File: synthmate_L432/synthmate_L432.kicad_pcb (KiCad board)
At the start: 2 copper layers, 5 parts, among them U1 STM32L432KCUx, U3 MIC5365-1.0YC5

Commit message: pcb_v1
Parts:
- added C3: 1uF, Capacitor_SMD:C_1206_3216Metric, F.Cu at (93.6, 54.4)
- added C4: 1uF, Capacitor_SMD:C_1206_3216Metric, F.Cu at (105.8, 56.7)
- added C5: 100nF, Capacitor_SMD:C_1206_3216Metric, F.Cu at (110.9, 56.8)
- added J1: USB_C_synthmate, Connector_USB:USB_C_Receptacle_GCT_USB4105-xx-A_16P_TopMnt_Horizontal, F.Cu at (94.7, 47.0)
- added J3: USB_C_connector_board, Connector_USB:USB_C_Receptacle_GCT_USB4105-xx-A_16P_TopMnt_Horizontal, F.Cu at (161.2, 47.2)
- added J5: Conn_01x16, Connector_PinSocket_2.54mm:PinSocket_1x15_P2.54mm_Vertical, F.Cu at (92.8, 60.2)
- added J6: Conn_01x13, Connector_PinSocket_2.54mm:PinSocket_1x13_P2.54mm_Vertical, F.Cu at (123.2, 33.8)
- added J7: Conn_01x04, Connector_PinSocket_2.54mm:PinSocket_1x04_P2.54mm_Vertical, F.Cu at (150.6, 43.3)
- added R1: 10k, Resistor_SMD:R_0805_2012Metric_Pad1.20x1.40mm_HandSolder, F.Cu at (116.0, 55.3)
- added R2: 5k1, Resistor_SMD:R_0805_2012Metric_Pad1.20x1.40mm_HandSolder, F.Cu at (92.5, 38.8)
- added R3: 5k1, Resistor_SMD:R_0805_2012Metric_Pad1.20x1.40mm_HandSolder, F.Cu at (96.0, 38.9)
- added R4: 1k, Resistor_SMD:R_0805_2012Metric_Pad1.20x1.40mm_HandSolder, F.Cu at (127.5, 38.0)
- added R5: 10k, Resistor_SMD:R_0805_2012Metric_Pad1.20x1.40mm_HandSolder, F.Cu at (116.3, 38.2)
- added SW1: RotaryEncoder_Switch, Rotary_Encoder:RotaryEncoder_Bourns_Vertical_PEC12R-3x17F-Sxxxx, F.Cu at (128.8, 44.5)
- added SW2: SW_Push, Button_Switch_THT:SW_TH_Tactile_Omron_B3F-10xx, F.Cu at (101.5, 50.2)
- added SW3: SW_Push, Button_Switch_THT:SW_TH_Tactile_Omron_B3F-10xx, F.Cu at (120.0, 50.2)
- added U2: USBLC6-2SC6, Package_TO_SOT_SMD:SOT-23-6, F.Cu at (106.0, 38.8)
- added U4: USBLC6-2SC6, Package_TO_SOT_SMD:SOT-23-6, F.Cu at (121.3, 55.5)
- C1: value 16V/47uF Tantalum -> 16V/47uF
- moved C2 74.9 mm to (100.7, 38.9)
- moved U3 67.5 mm to (98.1, 55.5)
- moved D1 63.0 mm to (121.8, 38.8)
- moved C1 58.8 mm to (105.7, 53.6), turned to 180 degrees
- moved U1 56.4 mm to (113.5, 45.9)
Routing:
- net 3V3: track 0.00 -> 124.1 mm, vias 0 -> 3
- net BOOT0: track 0.00 -> 110.6 mm, vias 0 -> 2
- net enc_A: track 0.00 -> 95.9 mm
- net USB_DM: track 0.00 -> 63.5 mm, vias 0 -> 1
- net NRST: track 0.00 -> 54.0 mm
- net enc_B: track 0.00 -> 53.0 mm, vias 0 -> 1
- net LPUART_TX: track 0.00 -> 47.6 mm, vias 0 -> 1
- net 5V: track 0.00 -> 45.0 mm, vias 0 -> 2
- net USB_DP: track 0.00 -> 37.0 mm, vias 0 -> 2
- net pushbutton_B: track 0.00 -> 32.3 mm, vias 0 -> 1
- net Net-(J1-SBU2): track 0.00 -> 31.9 mm
- net LPUART_RX: track 0.00 -> 31.5 mm, vias 0 -> 2
- net LED: track 0.00 -> 29.5 mm, vias 0 -> 1
- net adaptor_GND: track 0.00 -> 28.5 mm
- net Net-(J1-SBU1): track 0.00 -> 26.6 mm
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- added copper zone on B.Cu, net GND
- added copper zone on F.Cu, net GND
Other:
- board outline added: 74 x 30 mm
- board text added: "pcb cut"

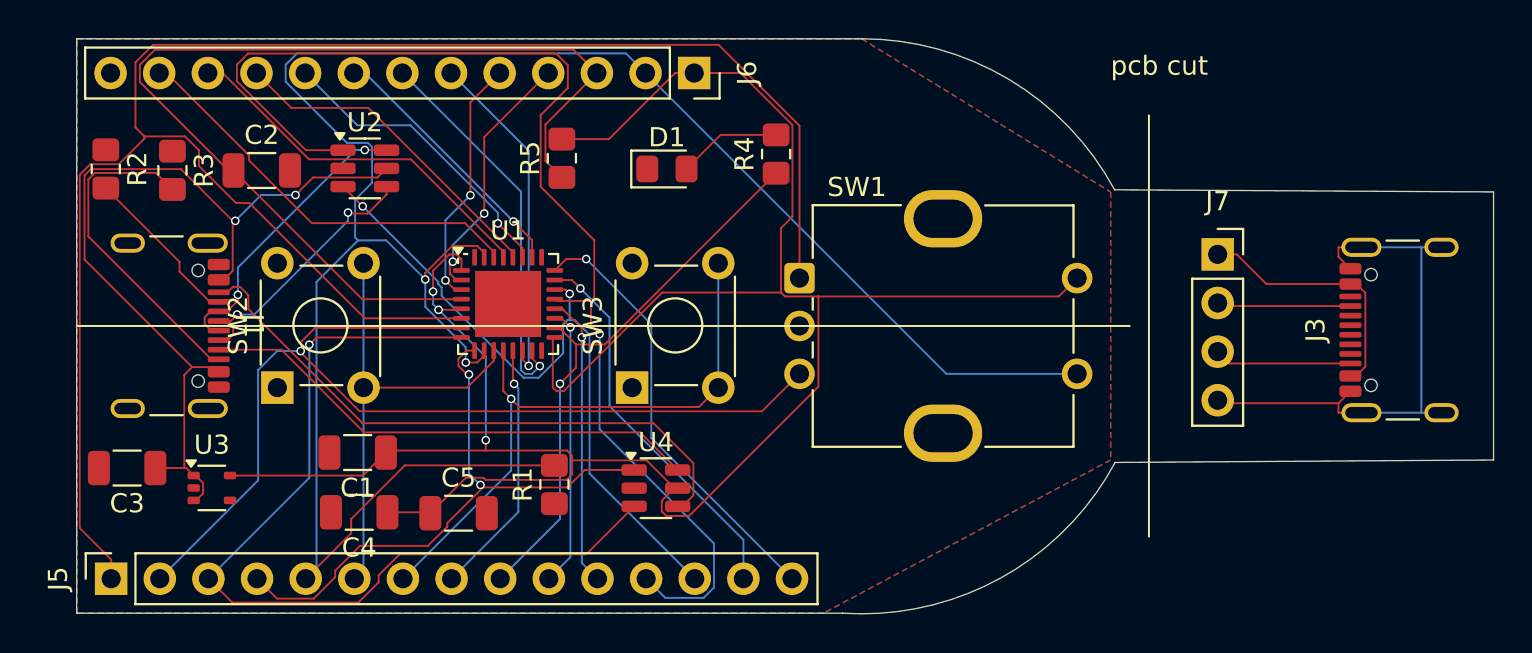
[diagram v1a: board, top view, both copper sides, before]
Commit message: switch to 4 layers, top layer signals routed
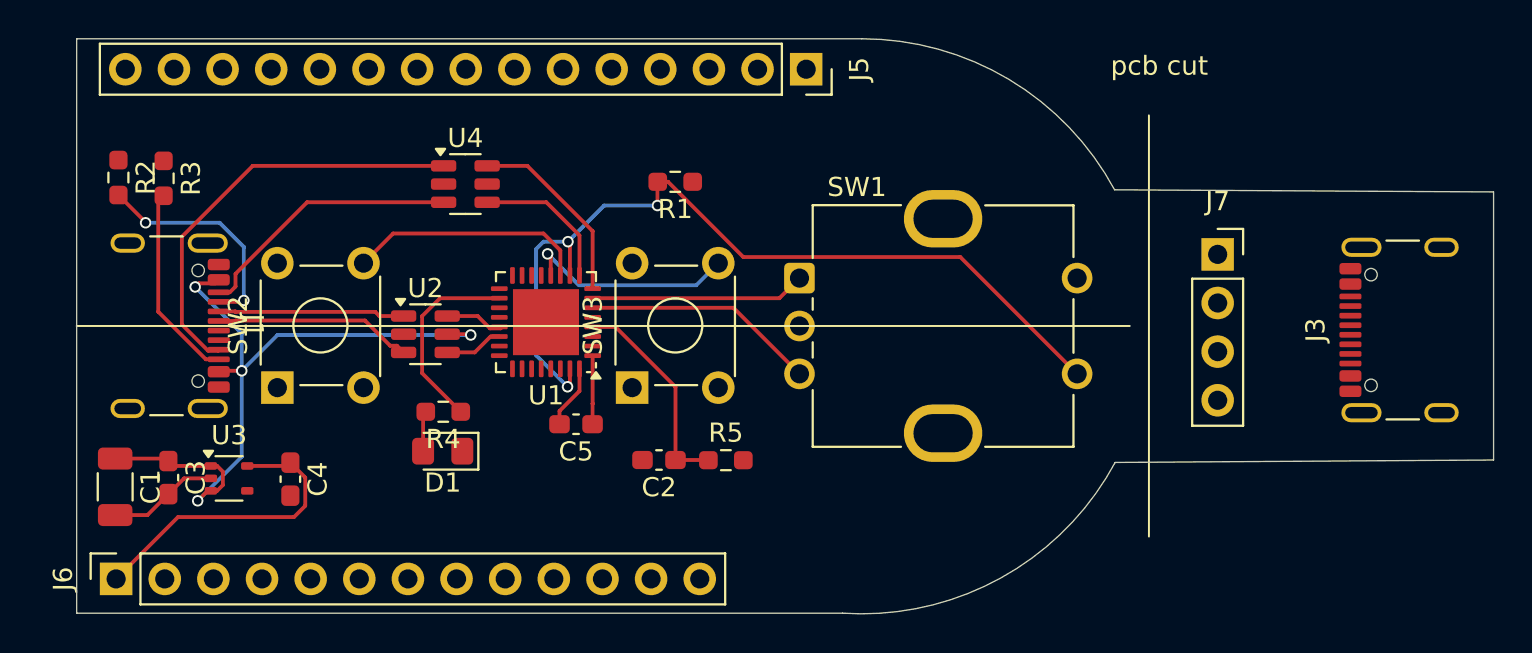
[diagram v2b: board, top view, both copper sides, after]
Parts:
- C2, C3, C4, C5: footprint Capacitor_SMD:C_1206_3216Metric -> Capacitor_SMD:C_0603_1608Metric_Pad1.08x0.95mm_HandSolder
- R1, R2, R3, R4, R5: footprint Resistor_SMD:R_0805_2012Metric_Pad1.20x1.40mm_HandSolder -> Resistor_SMD:R_0603_1608Metric_Pad0.98x0.95mm_HandSolder
- moved J5 45.0 mm to (129.1, 33.6), turned to -90 degrees
- moved J6 40.1 mm to (93.1, 60.2), turned to 90 degrees
- moved C2 25.7 mm to (121.4, 54.0), turned to 180 degrees
- moved R4 22.0 mm to (110.1, 51.5), turned to 180 degrees
- moved D1 18.8 mm to (110.1, 53.5), turned to 180 degrees
- moved U4 18.7 mm to (111.3, 39.6)
- moved R5 17.9 mm to (124.9, 54.0), turned to 0 degrees
- moved R1 17.0 mm to (122.3, 39.5), turned to 180 degrees
- moved C1 12.8 mm to (93.0, 55.4), turned to -90 degrees
- moved U2 9.22 mm to (109.2, 47.4)
- moved C5 7.70 mm to (117.1, 52.1), turned to 180 degrees
- moved C4 3.99 mm to (102.2, 55.0), turned to -90 degrees
- moved C3 2.21 mm to (95.8, 54.9), turned to -90 degrees
- moved U1 2.19 mm to (115.5, 46.8), turned to 180 degrees
- moved U3 1.03 mm to (99.0, 55.0)
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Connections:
- C1 pad 1: 3V3 -> 5V
- J1 pad A6: Net-(J1-D+-PadA6) -> /usb_P
- J1 pad A7: Net-(J1-D--PadA7) -> /usb_N
- J1 pad B6: Net-(J1-D+-PadA6) -> /usb_P
- J1 pad B7: Net-(J1-D--PadA7) -> /usb_N
- J5 pad 1: enc_A -> unconnected-(J5-Pin_1-Pad1)
- J5 pad 10: USART1_TX -> unconnected-(J5-Pin_10-Pad10)
- J5 pad 11: USART1_RX -> unconnected-(J5-Pin_11-Pad11)
- J5 pad 12: USB_DM -> unconnected-(J5-Pin_12-Pad12)
- J5 pad 13: USB_DP -> unconnected-(J5-Pin_13-Pad13)
- J5 pad 14: PA13 -> unconnected-(J5-Pin_14-Pad14)
- J5 pad 15: PA14 -> unconnected-(J5-Pin_15-Pad15)
- J5 pad 2: enc_B -> unconnected-(J5-Pin_2-Pad2)
- J5 pad 3: LPUART_TX -> unconnected-(J5-Pin_3-Pad3)
- J5 pad 4: LPUART_RX -> unconnected-(J5-Pin_4-Pad4)
- J5 pad 5: BOOT0 -> unconnected-(J5-Pin_5-Pad5)
- J5 pad 6: pushbutton_A -> unconnected-(J5-Pin_6-Pad6)
- J5 pad 7: pushbutton_B -> unconnected-(J5-Pin_7-Pad7)
- J5 pad 8: PA7 -> unconnected-(J5-Pin_8-Pad8)
- J5 pad 9: LED -> unconnected-(J5-Pin_9-Pad9)
- J6 pad 1: 3V3 -> unconnected-(J6-Pin_1-Pad1)
- J6 pad 10: PB5 -> unconnected-(J6-Pin_10-Pad10)
- J6 pad 11: PB6 -> unconnected-(J6-Pin_11-Pad11)
- J6 pad 12: PB7 -> unconnected-(J6-Pin_12-Pad12)
- J6 pad 13: GND -> unconnected-(J6-Pin_13-Pad13)
- J6 pad 2: BOOT0 -> unconnected-(J6-Pin_2-Pad2)
- J6 pad 3: NRST -> unconnected-(J6-Pin_3-Pad3)
- J6 pad 4: PC14 -> unconnected-(J6-Pin_4-Pad4)
- J6 pad 5: PC15 -> unconnected-(J6-Pin_5-Pad5)
- J6 pad 6: PB0 -> unconnected-(J6-Pin_6-Pad6)
- J6 pad 7: PB1 -> unconnected-(J6-Pin_7-Pad7)
- J6 pad 8: PB3 -> unconnected-(J6-Pin_8-Pad8)
- J6 pad 9: PB4 -> unconnected-(J6-Pin_9-Pad9)
- U1 pad 21: USB_DM -> /usb-
- U1 pad 22: USB_DP -> /usb+
- U1 pad 6: enc_A -> enc_B
- U1 pad 7: enc_B -> enc_A
- U2 pad 1: USB_DM -> /usb_N
- U2 pad 3: USB_DP -> /usb_P
- U2 pad 4: Net-(J1-D+-PadA6) -> /usb+
- U2 pad 6: Net-(J1-D--PadA7) -> /usb-
- U4 pad 1: LPUART_RX -> Net-(J1-SBU1)
- U4 pad 3: LPUART_TX -> Net-(J1-SBU2)
- U4 pad 4: Net-(J1-SBU2) -> LPUART_RX
- U4 pad 6: Net-(J1-SBU1) -> LPUART_TX
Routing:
- net 3V3: track 124.1 -> 19.9 mm, vias 3 -> 0
- net enc_A: track 95.9 -> 11.2 mm
- net BOOT0: track 110.6 -> 45.2 mm, vias 2 -> 3
- net USB_DM: track 63.5 -> 0.00 mm, vias 1 -> 0
- net NRST: track 54.0 -> 11.2 mm
- net enc_B: track 53.0 -> 12.2 mm, vias 1 -> 0
- net LPUART_TX: track 47.6 -> 9.92 mm, vias 1 -> 0
- net USB_DP: track 37.0 -> 0.00 mm, vias 2 -> 0
- net adaptor_GND: track 28.5 -> 0.00 mm
- net LPUART_RX: track 31.5 -> 7.63 mm, vias 2 -> 0
- net PA14: track 23.0 -> 0.00 mm, vias 1 -> 0
- net PB7: track 21.8 -> 0.00 mm
- net pushbutton_B: track 32.3 -> 11.3 mm
- net PB1: track 20.3 -> 0.00 mm, vias 1 -> 0
- net PA13: track 20.2 -> 0.00 mm, vias 1 -> 0
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- added copper zone on In2.Cu, net 3V3
- added copper zone on In1.Cu, net GND
- removed copper zone on B.Cu, net GND
- removed copper zone on F.Cu, net GND
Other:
- copper layers 2 -> 4

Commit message: added debounce
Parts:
- added C10: 100nF, Capacitor_SMD:C_0603_1608Metric_Pad1.08x0.95mm_HandSolder, F.Cu at (134.6, 87.0)
- added C6: 100nF, Capacitor_SMD:C_0603_1608Metric_Pad1.08x0.95mm_HandSolder, F.Cu at (134.6, 77.0)
- added C7: 100nF, Capacitor_SMD:C_0603_1608Metric_Pad1.08x0.95mm_HandSolder, F.Cu at (134.6, 79.5)
- added C8: 100nF, Capacitor_SMD:C_0603_1608Metric_Pad1.08x0.95mm_HandSolder, F.Cu at (134.6, 82.0)
- added C9: 100nF, Capacitor_SMD:C_0603_1608Metric_Pad1.08x0.95mm_HandSolder, F.Cu at (134.6, 84.5)
- added R10: 10k, Resistor_SMD:R_0603_1608Metric_Pad0.98x0.95mm_HandSolder, F.Cu at (139.0, 87.0)
- added R11: 10k, Resistor_SMD:R_0603_1608Metric_Pad0.98x0.95mm_HandSolder, F.Cu at (143.3, 77.0)
- added R12: 10k, Resistor_SMD:R_0603_1608Metric_Pad0.98x0.95mm_HandSolder, F.Cu at (143.3, 79.5)
- added R13: 10k, Resistor_SMD:R_0603_1608Metric_Pad0.98x0.95mm_HandSolder, F.Cu at (143.3, 82.0)
- added R14: 10k, Resistor_SMD:R_0603_1608Metric_Pad0.98x0.95mm_HandSolder, F.Cu at (143.3, 84.5)
- added R6: 10k, Resistor_SMD:R_0603_1608Metric_Pad0.98x0.95mm_HandSolder, F.Cu at (139.0, 77.0)
- added R7: 10k, Resistor_SMD:R_0603_1608Metric_Pad0.98x0.95mm_HandSolder, F.Cu at (139.0, 79.5)
- added R8: 10k, Resistor_SMD:R_0603_1608Metric_Pad0.98x0.95mm_HandSolder, F.Cu at (139.0, 82.0)
- added R9: 10k, Resistor_SMD:R_0603_1608Metric_Pad0.98x0.95mm_HandSolder, F.Cu at (139.0, 84.5)
- added U5: 40106, Package_SO:TSSOP-14_4.4x5mm_P0.65mm, F.Cu at (131.2, 57.2)
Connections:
- R1 pad 2: BOOT0 -> Net-(C10-Pad1)
- SW1 pad A: enc_A -> Net-(C6-Pad1)
- SW1 pad B: enc_B -> Net-(C7-Pad1)
- SW1 pad S1: 3V3 -> Net-(C10-Pad1)
- SW1 pad S2: BOOT0 -> 3V3
- SW2 pad 2: pushbutton_A -> Net-(C8-Pad1)
- SW3 pad 2: pushbutton_B -> Net-(C9-Pad1)

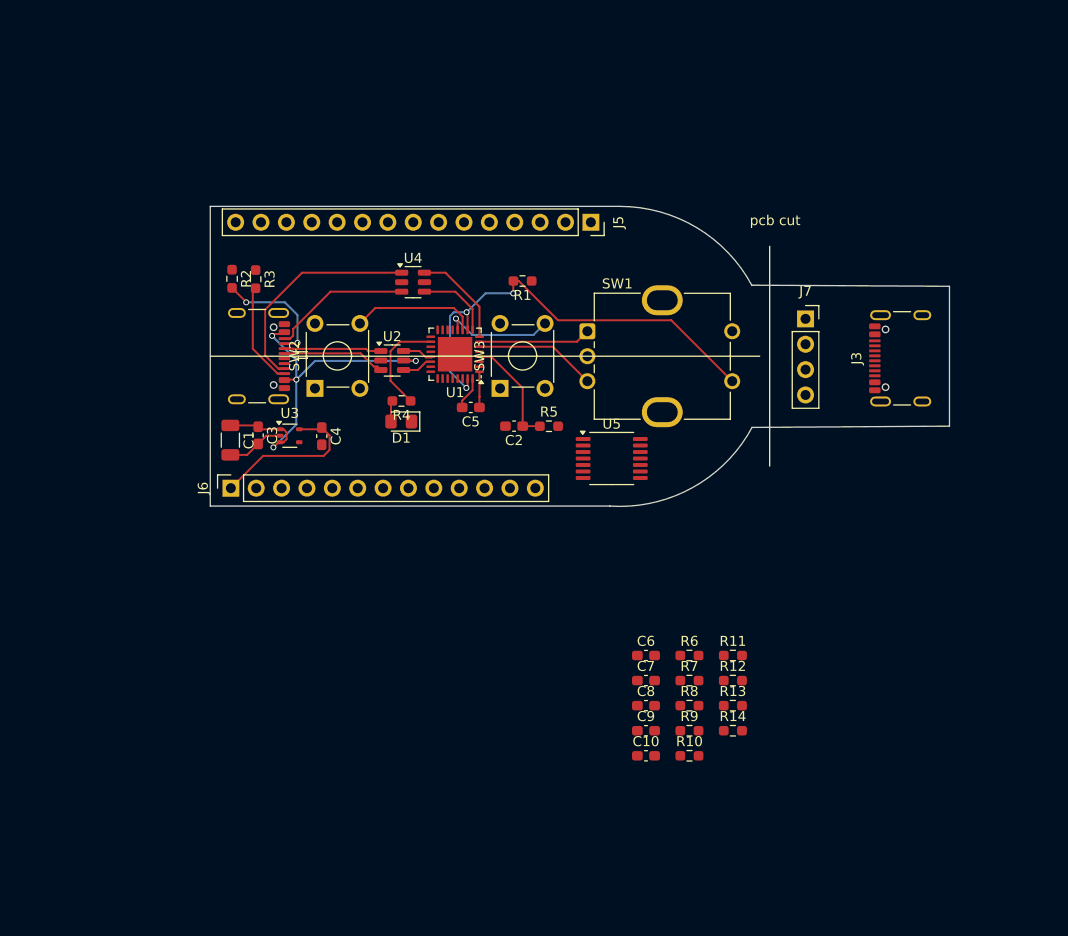
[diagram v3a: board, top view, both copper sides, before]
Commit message: pcb outline
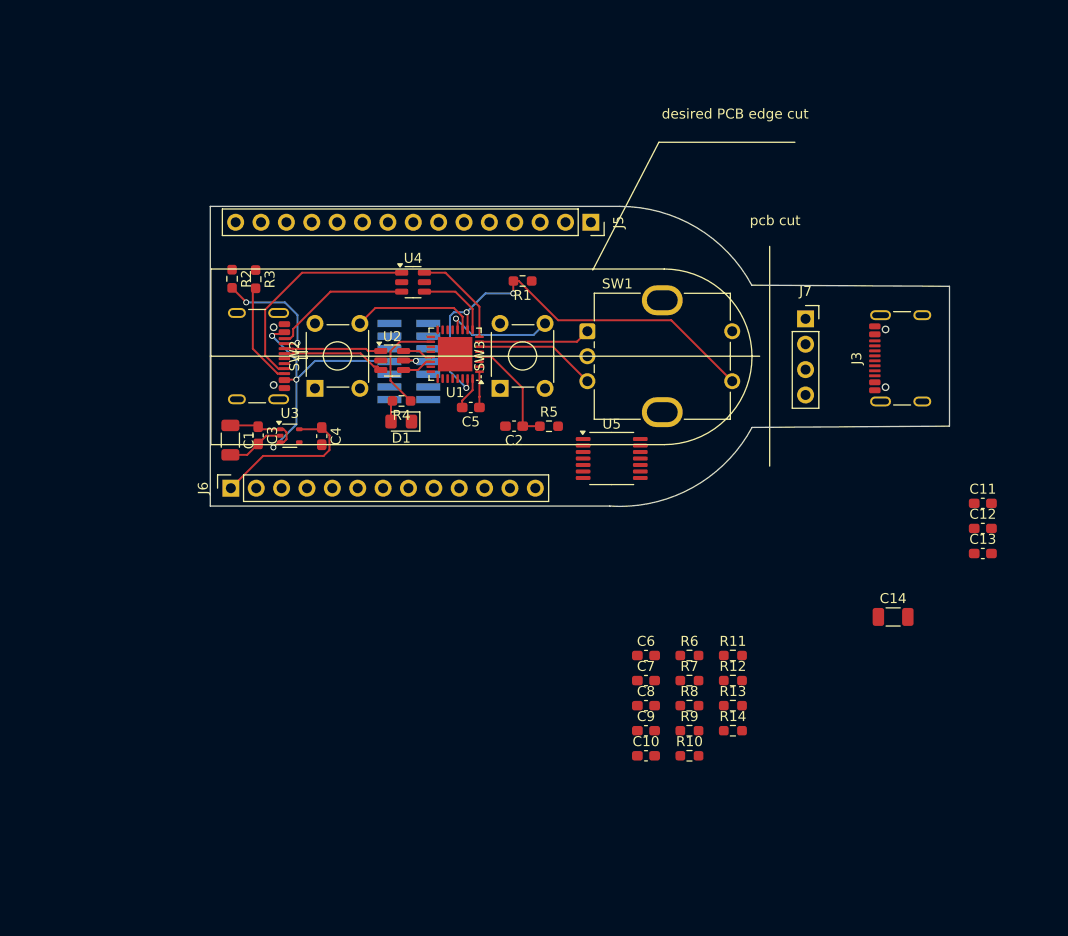
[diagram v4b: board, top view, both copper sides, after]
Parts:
- added C11: 100nF, Capacitor_SMD:C_0603_1608Metric_Pad1.08x0.95mm_HandSolder, F.Cu at (168.3, 61.7)
- added C12: 100nF, Capacitor_SMD:C_0603_1608Metric_Pad1.08x0.95mm_HandSolder, F.Cu at (168.3, 64.2)
- added C13: 1uF, Capacitor_SMD:C_0603_1608Metric_Pad1.08x0.95mm_HandSolder, F.Cu at (168.3, 66.8)
- added C14: 16V/47uF, Capacitor_SMD:C_1206_3216Metric, F.Cu at (159.4, 73.1)
- added J8: Conn_ST_STDC14, Connector_PinHeader_1.27mm:PinHeader_2x07_P1.27mm_Vertical_SMD, B.Cu at (110.9, 47.5)
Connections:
- R1 pad 1: GND -> Net-(R1-Pad1)
- R1 pad 2: Net-(C10-Pad1) -> 3V3
- R10 pad 1: Net-(C8-Pad1) -> Net-(R10-Pad1)
- R11 pad 1: Net-(C9-Pad1) -> Net-(R11-Pad1)
- R12 pad 1: Net-(C8-Pad1) -> Net-(R10-Pad1)
- R12 pad 2: Net-(R12-Pad2) -> Net-(C8-Pad1)
- R13 pad 1: Net-(C9-Pad1) -> Net-(R11-Pad1)
- R13 pad 2: Net-(R13-Pad2) -> Net-(C9-Pad1)
- R14 pad 1: Net-(R14-Pad1) -> Net-(C10-Pad1)
- R14 pad 2: Net-(C10-Pad1) -> Net-(R1-Pad1)
- R6 pad 1: Net-(C7-Pad1) -> Net-(R6-Pad1)
- R7 pad 1: Net-(C6-Pad1) -> Net-(R7-Pad1)
- R8 pad 1: Net-(R8-Pad1) -> Net-(C6-Pad1)
- R8 pad 2: Net-(C6-Pad1) -> Net-(R7-Pad1)
- R9 pad 1: Net-(R9-Pad1) -> Net-(C7-Pad1)
- R9 pad 2: Net-(C7-Pad1) -> Net-(R6-Pad1)
- SW1 pad A: Net-(C6-Pad1) -> Net-(R7-Pad1)
- SW1 pad B: Net-(C7-Pad1) -> Net-(R6-Pad1)
- SW1 pad S1: Net-(C10-Pad1) -> Net-(R1-Pad1)
- SW1 pad S2: 3V3 -> GND
- SW2 pad 2: Net-(C8-Pad1) -> Net-(R10-Pad1)
- SW3 pad 2: Net-(C9-Pad1) -> Net-(R11-Pad1)
- U5 pad 1: Net-(R8-Pad1) -> Net-(C6-Pad1)
- U5 pad 11: Net-(R13-Pad2) -> Net-(C9-Pad1)
- U5 pad 13: unconnected-(U5-Pad13) -> GND
- U5 pad 3: Net-(R9-Pad1) -> Net-(C7-Pad1)
- U5 pad 5: Net-(R14-Pad1) -> Net-(C10-Pad1)
- U5 pad 9: Net-(R12-Pad2) -> Net-(C8-Pad1)
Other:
- board text added: "desired PCB edge cut"
